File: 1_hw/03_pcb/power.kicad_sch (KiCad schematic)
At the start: 0 parts

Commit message: FEAT: Added +15V and -15V Regulator. Replaced some Symbols to add additional Part Number Field.
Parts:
- added C? (x2): 6.8p, symbol Device:C_Small
- added C? (x10): 4.7u, symbol Device:C_Small
- added C? (x3): 0.1u, symbol Device:C_Small
- added C?: 0.22u, symbol Device:C_Small
- added C?: 4700p, symbol Device:C_Small
- added C?: 1u, symbol Device:C_Small
- added C?: 0.01u, symbol Device:C_Small
- added C?: 10u, symbol Device:C_Small
- added C?: C_Polarized_Small_US, symbol Device:C_Polarized_Small_US
- added D? (x2): MBRM120ET1G, BRZK_TBD, symbol BRZK_DIODE:MBRM120ET1G
- added L? (x2): 4.7u, symbol Device:L_Small
- added R?: 976k, symbol Device:R_Small_US
- added R?: 104.8k, symbol Device:R_Small_US
- added R?: 1.30M, symbol Device:R_Small_US
- added R? (x6): 0, symbol Device:R_Small_US
- added R?: 110k, symbol Device:R_Small_US
- added R?: 85.8k, symbol Device:R_Small_US
- added U?: TPS65131RGE, Package_DFN_QFN:VQFN-24-1EP_4x4mm_P0.5mm_EP2.45x2.45mm_ThermalVias, symbol Regulator_Switching:TPS65131RGE
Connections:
- new net: R?.1, R?.1, R?.2
- new net: C?.2, R?.1, R?.2, U?.22 (FBP)
- new net: C?.1, R?.1, R?.2, U?.16 (FBN)
- new net: C?.2, R?.1
- new net: C?.1, R?.1, U?.17 (VREF)
- new net: D?.2 (A), L?.2, U?.1 (INP), U?.24 (INP)
- new net: C?.1, R?.2, U?.10 (ENN), U?.11 (PSN), U?.4 (VIN), U?.8 (ENP), U?.9 (PSP)
- new net: D?.1 (K), L?.2, U?.13 (OUTN), U?.14 (OUTN)
- new net: R?.1, R?.2, R?.2
- new net: C?.1, R?.2 (x3)
- new net: R?.1, U?.21 (CP)
- new net: R?.1, U?.18 (CN)
- new net 15P0V_A: C?.1, C?.1, C?.1, C?.1, C?.1, D?.1 (K), R?.1, U?.23 (VPOS)
- new net 5P0V: C?.1, C?.1, C?.1, C?.1, L?.1, R?.1, U?.5 (INN), U?.6 (INN)
- new net GND: C?.2, C?.2, C?.2, C?.2, C?.2, C?.2, C?.2, C?.2, C?.2, C?.2, C?.2, C?.2, C?.2, C?.2, C?.2, C?.2, C?.2, C?.2, L?.1, R?.2, U?.19 (AGND), U?.2 (PGND), U?.25 (EP), U?.3 (PGND)
- new net N15P0V_A: C?.1, C?.1, C?.1, C?.1, C?.1, D?.2 (A), R?.2, U?.15 (VNEG)
- no-connect marks 0 -> 1
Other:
- note added: "+15V & -15V SWITCHING REGULATOR"
- note added: "BULK CAPACITORS"

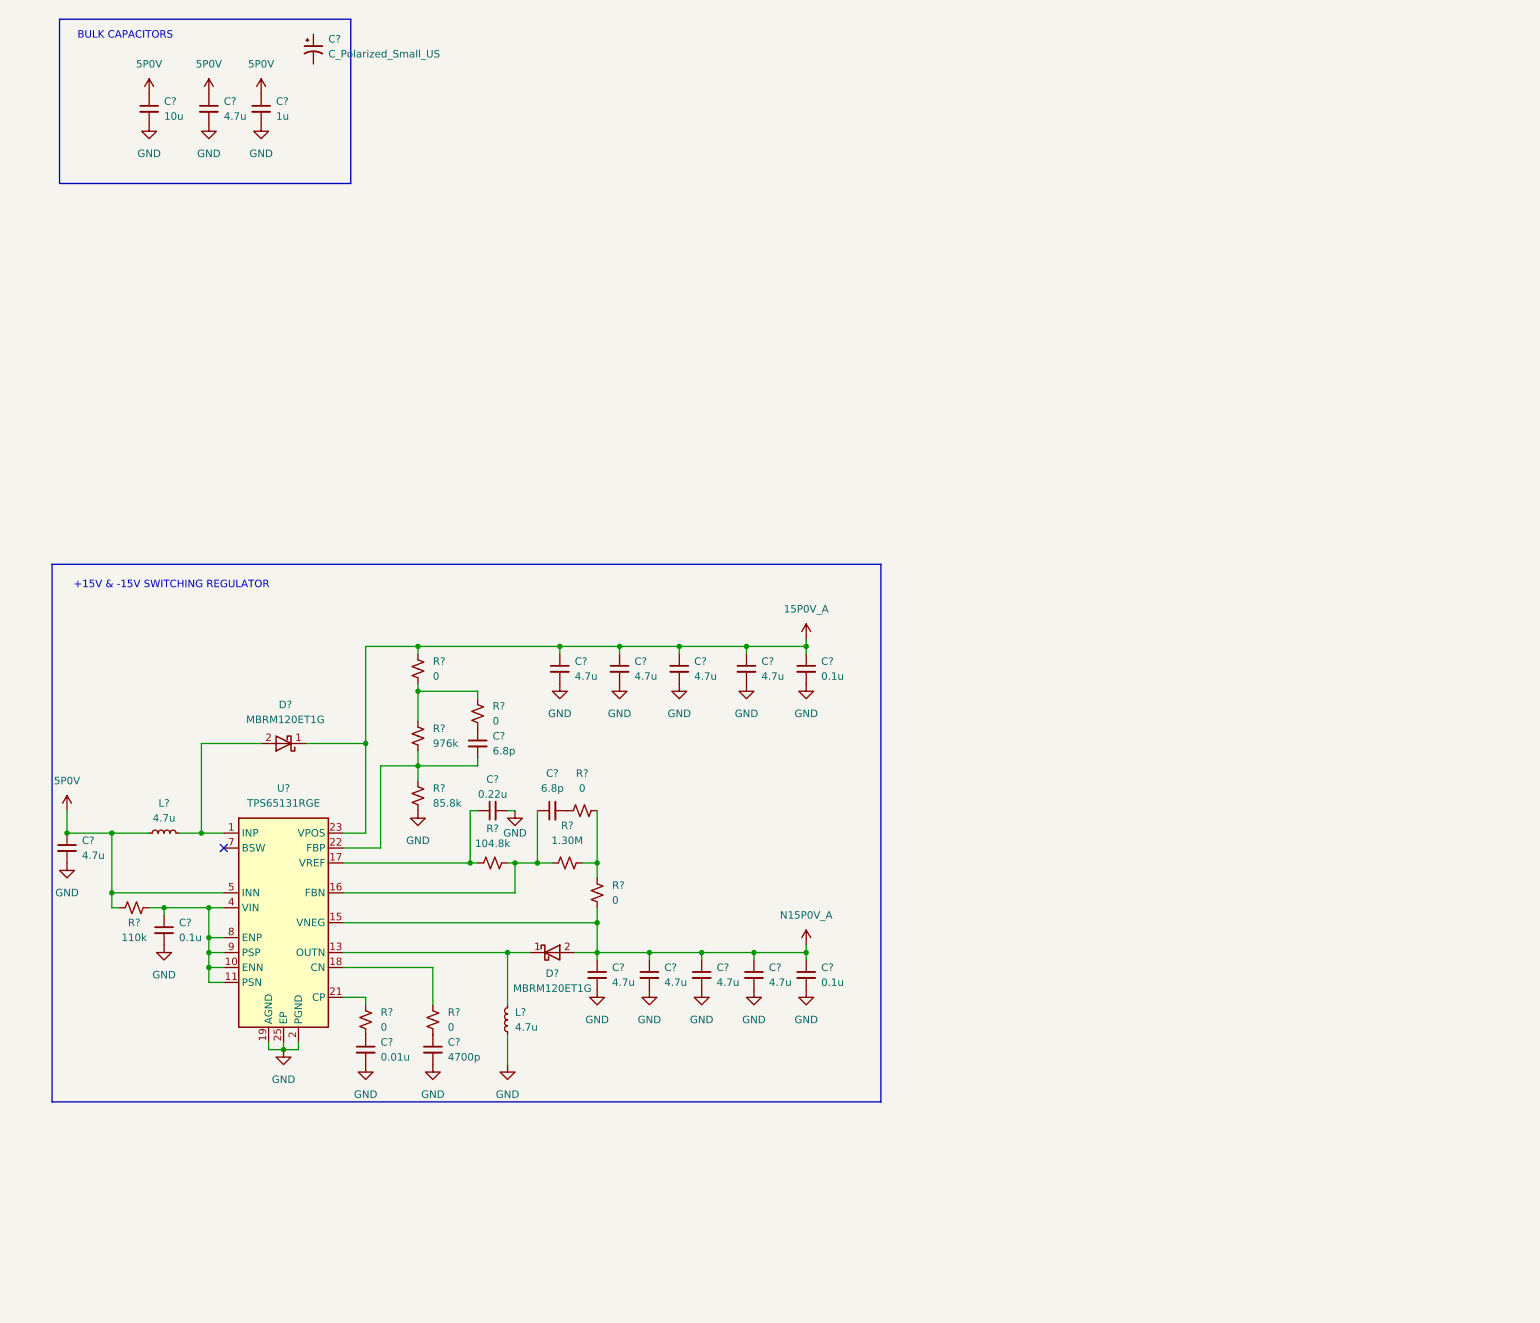
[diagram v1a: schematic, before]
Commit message: FEAT: Added USB ESD Protection.
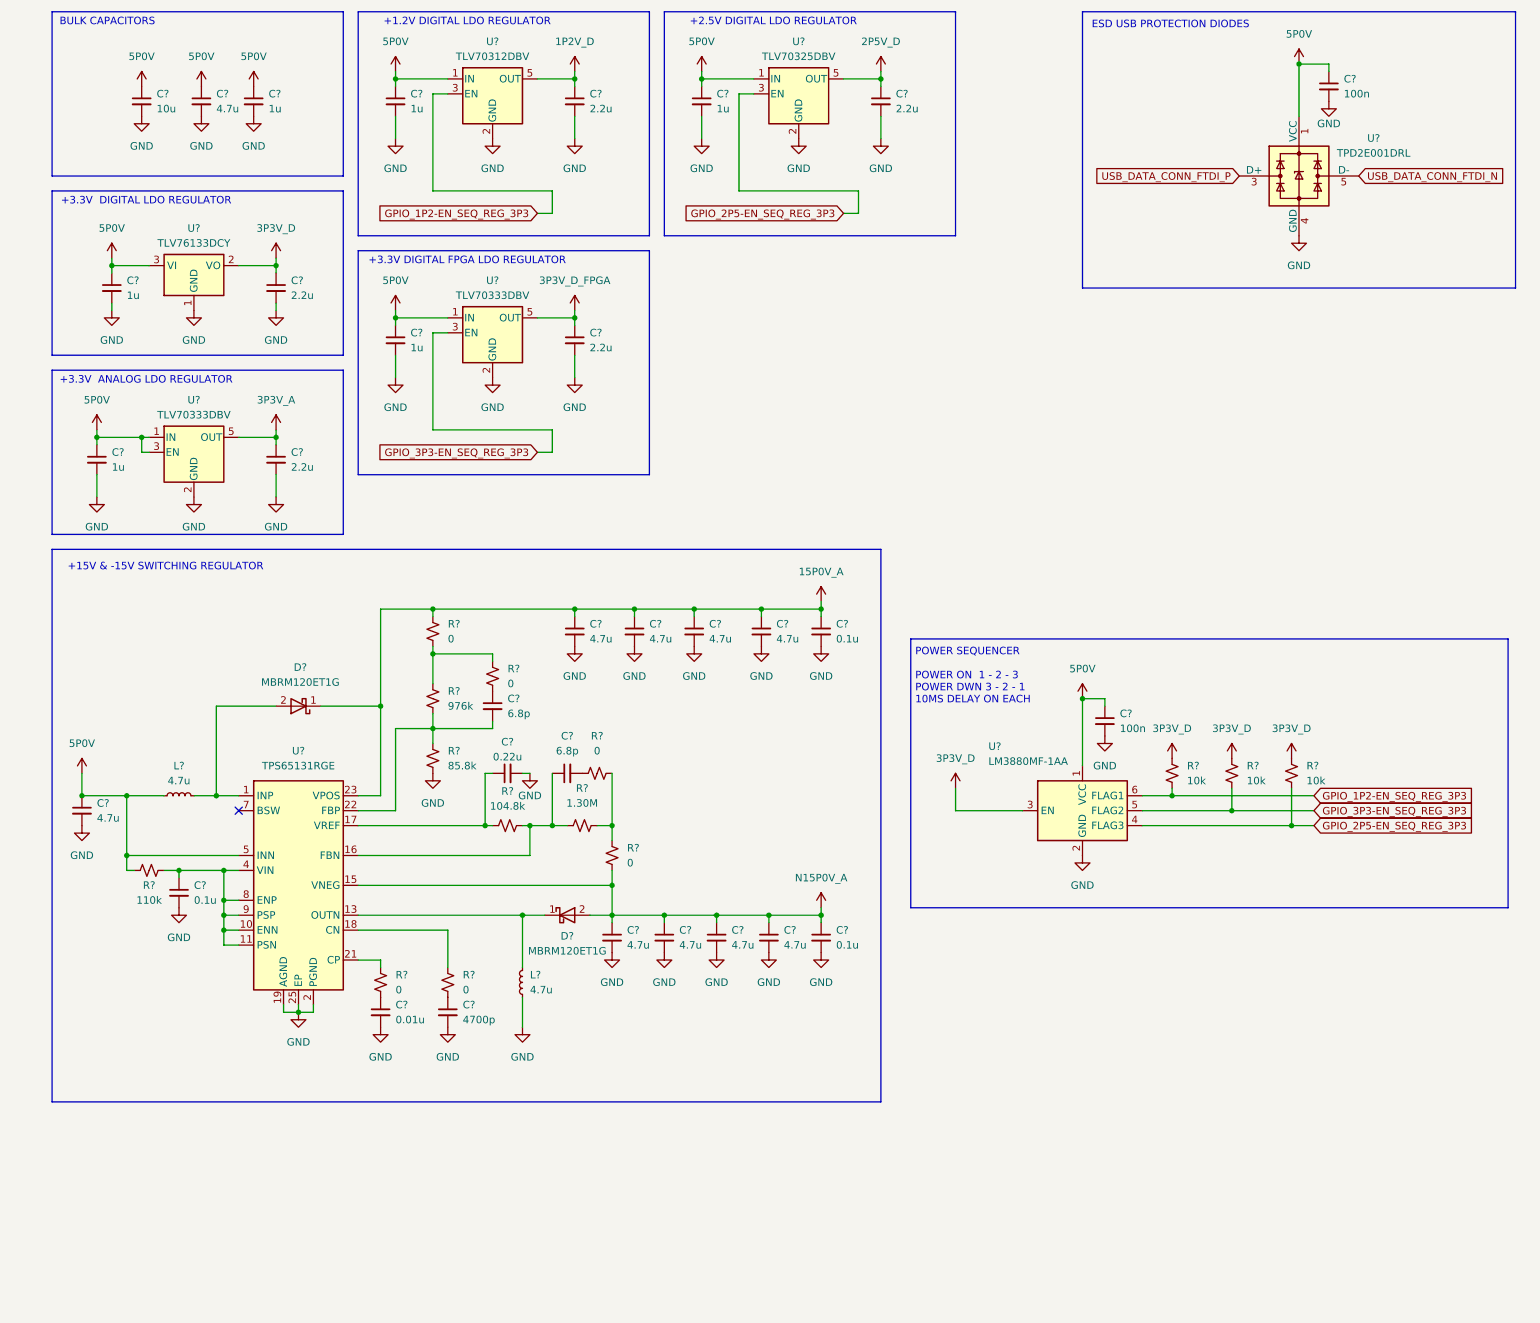
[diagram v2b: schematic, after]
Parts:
- removed C?: C_Polarized_Small_US, symbol Device:C_Polarized_Small_US
- removed U?: TPS65131RGE, Package_DFN_QFN:VQFN-24-1EP_4x4mm_P0.5mm_EP2.45x2.45mm_ThermalVias, symbol Regulator_Switching:TPS65131RGE
- added C? (x5): 2.2u, symbol Device:C_Small
- added C? (x5): 1u, symbol Device:C_Small
- added C? (x2): 100n, Capacitor_SMD:C_0603_1608Metric, symbol Device:C_Small
- added R? (x3): 10k, Resistor_SMD:R_0603_1608Metric, symbol Device:R_Small_US
- added U?: TPD2E001DRL, Package_TO_SOT_SMD:SOT-553, symbol BRZK_DIODE:TPD2E001DRL
- added U? (x2): TLV70333DBV, Package_TO_SOT_SMD:SOT-23-5, symbol BRZK_POWER:TLV70333DBV
- added U?: TLV70325DBV, Package_TO_SOT_SMD:SOT-23-5, symbol BRZK_POWER:TLV70325DBV
- added U?: TLV70312DBV, Package_TO_SOT_SMD:SOT-23-5, symbol BRZK_POWER:TLV70312DBV
- added U?: TLV76133DCY, Package_TO_SOT_SMD:SOT-223-3_TabPin2, symbol BRZK_POWER:TLV76133DCY
- added U?: LM3880MF-1AA, Package_TO_SOT_SMD:SOT-23-6, symbol Power_Supervisor:LM3880
- added U?: TPS65131RGE, Package_DFN_QFN:VQFN-24-1EP_4x4mm_P0.5mm_EP2.45x2.45mm_ThermalVias, symbol BRZK_POWER:TPS65131RGE
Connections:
- net 15P0V_A: now also U?.23 (VPOS)
- net 5P0V: now also C?.1, C?.1, C?.1, C?.1, C?.1, C?.1, C?.1, U?.1 (IN), U?.1 (IN), U?.1 (IN), U?.1 (IN), U?.1 (VCC), U?.1 (VCC), U?.3 (EN), U?.3 (VI), U?.5 (INN), U?.6 (INN)
- net GND: now also C?.2, C?.2, C?.2, C?.2, C?.2, C?.2, C?.2, C?.2, C?.2, C?.2, C?.2, C?.2, U?.1 (GND), U?.19 (AGND), U?.2 (GND), U?.2 (GND), U?.2 (GND), U?.2 (GND), U?.2 (GND), U?.2 (PGND), U?.25 (EP), U?.3 (PGND), U?.4 (GND)
- net N15P0V_A: now also U?.15 (VNEG)
- net at C?.2, R?.1, R?.2: now also U?.22 (FBP)
- net at C?.1, R?.1, R?.2: now also U?.16 (FBN)
- net at C?.1, R?.1: now also U?.17 (VREF)
- net at D?.2 (A), L?.2: now also U?.1 (INP), U?.24 (INP)
- net at C?.1, R?.2: now also U?.10 (ENN), U?.11 (PSN), U?.4 (VIN), U?.8 (ENP), U?.9 (PSP)
- net at D?.1 (K), L?.2: now also U?.13 (OUTN), U?.14 (OUTN)
- net at R?.1: now also U?.21 (CP)
- net at R?.1: now also U?.18 (CN)
- new net 1P2V_D: C?.1, U?.5 (OUT)
- new net 2P5V_D: C?.1, U?.5 (OUT)
- new net 3P3V_A: C?.1, U?.5 (OUT)
- new net 3P3V_D: C?.1, R?.2, R?.2, R?.2, U?.2 (VO), U?.3 (EN)
- new net 3P3V_D_FPGA: C?.1, U?.5 (OUT)
- new net GPIO_1P2-EN_SEQ_REG_3P3: R?.1, U?.3 (EN), U?.6 (FLAG1)
- new net GPIO_2P5-EN_SEQ_REG_3P3: R?.1, U?.3 (EN), U?.4 (FLAG3)
- new net GPIO_3P3-EN_SEQ_REG_3P3: R?.1, U?.3 (EN), U?.5 (FLAG2)
- new net USB_DATA_CONN_FTDI_N: U?.5 (D-)
- new net USB_DATA_CONN_FTDI_P: U?.3 (D+)
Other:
- note added: "+1.2V DIGITAL LDO REGULATOR"
- note added: "+2.5V DIGITAL LDO REGULATOR"
- note added: "+3.3V ANALOG LDO REGULATOR"
- note added: "+3.3V DIGITAL FPGA LDO REGULATOR"
- note added: "+3.3V DIGITAL LDO REGULATOR"
- note added: "ESD USB PROTECTION DIODES"
- note added: "POWER SEQUENCER POWER ON 1 - 2 - 3 POWER DWN 3 - 2 - 1 10MS DELAY ON EACH"
- moved on the sheet: C?, D?, L?, R?

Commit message: FEAT: Added Clocking Sheet, FPGA Flash, and FPGA Decoupling.
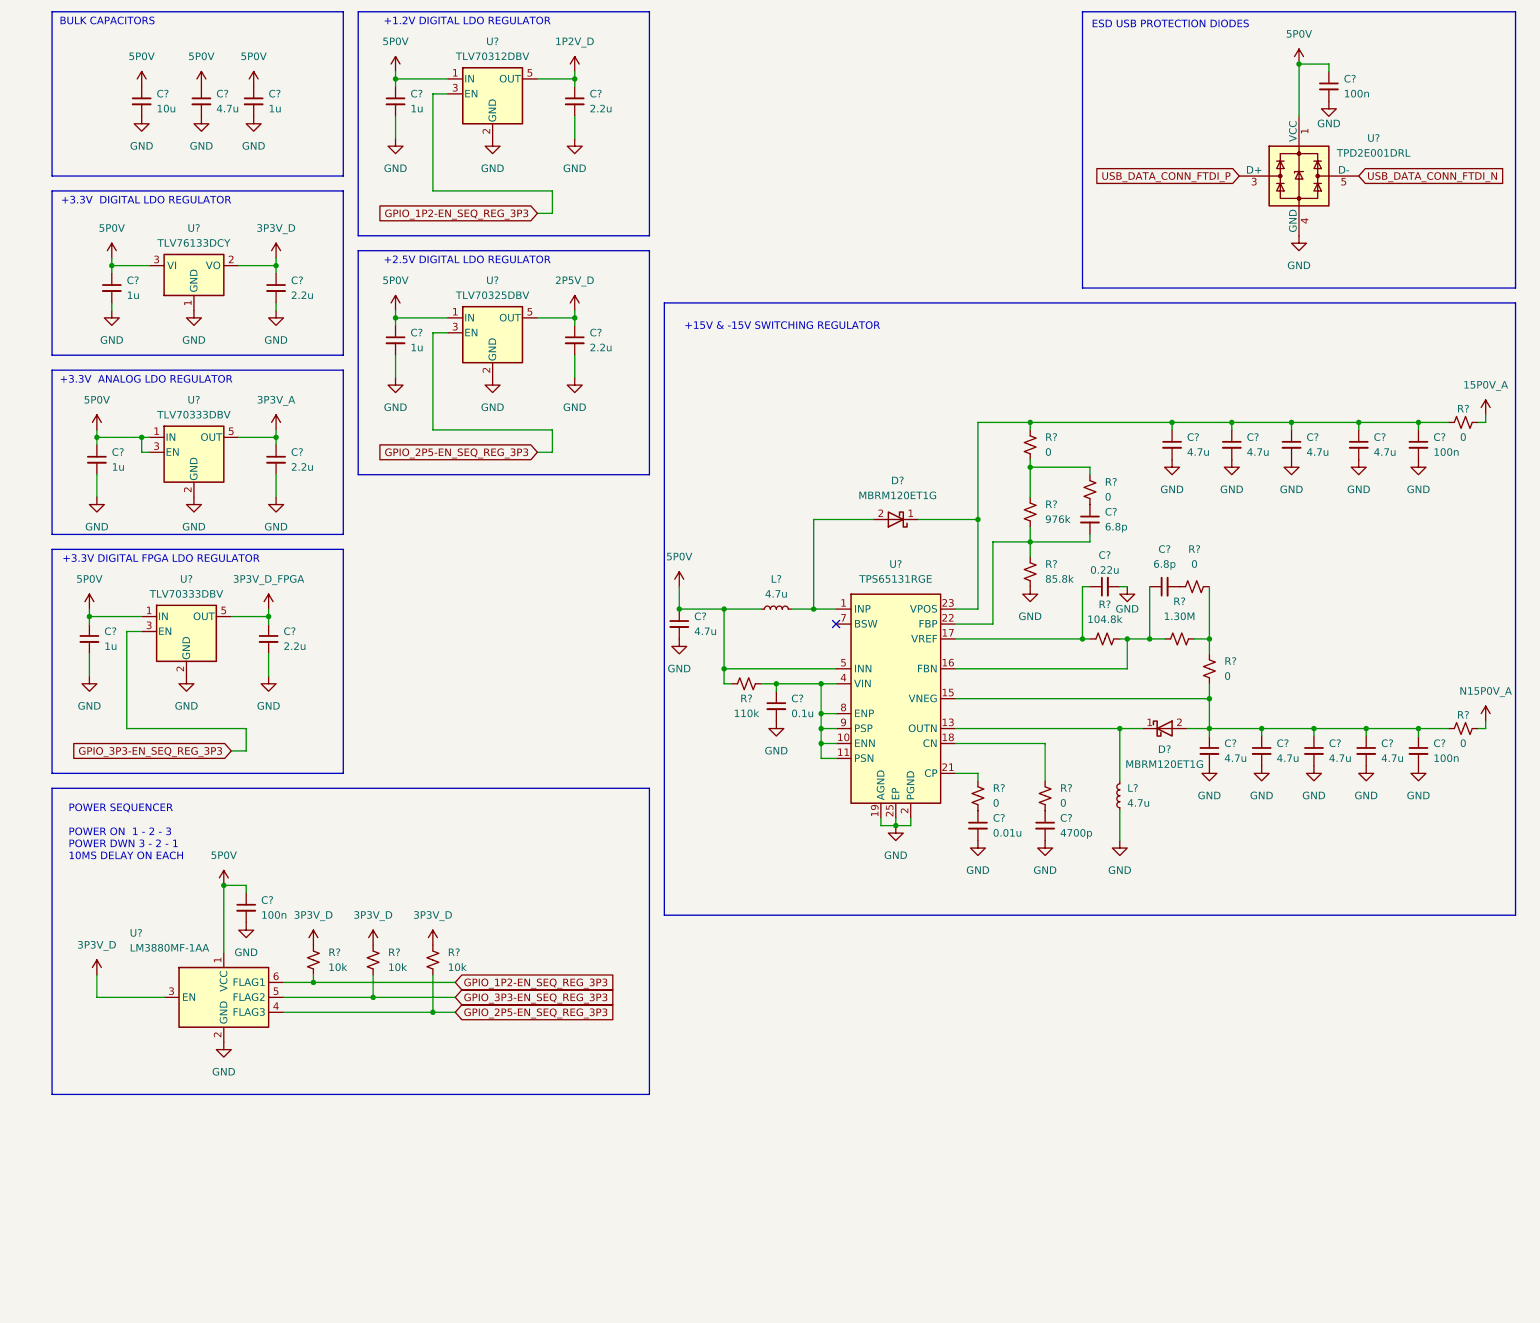
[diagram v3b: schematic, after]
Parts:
- added R? (x2): 0, Resistor_SMD:R_0603_1608Metric, symbol Device:R_Small_US
- C? (x2): value 0.1u -> 100n
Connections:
- net 15P0V_A: now also R?.1; no longer C?.1, C?.1, C?.1, C?.1, C?.1, D?.1 (K), R?.1, U?.23 (VPOS)
- net N15P0V_A: now also R?.1; no longer C?.1, C?.1, C?.1, C?.1, C?.1, D?.2 (A), R?.2, U?.15 (VNEG)
- new net: C?.1, C?.1, C?.1, C?.1, C?.1, D?.1 (K), R?.1, R?.2, U?.23 (VPOS)
- new net: C?.1, C?.1, C?.1, C?.1, C?.1, D?.2 (A), R?.2, R?.2, U?.15 (VNEG)
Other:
- moved on the sheet: C?, D?, L?, R?, U?

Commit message: FEAT: Added Connectors on Schematic. Created Connector Footprints.
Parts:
- added R?: 1M, symbol Device:R_Small_US
- gave numbers to parts that had none: 60
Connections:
- net GND: now also R?.2
- new net C_GND: R?.1
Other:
- note added: "BLEED RESISTOR"
